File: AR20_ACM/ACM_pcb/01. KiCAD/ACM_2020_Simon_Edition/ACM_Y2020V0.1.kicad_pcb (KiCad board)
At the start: 2 copper layers, 18 x 22.5 mm, 32 parts, among them J1 TC2030-MCP-NL, P1 Conn_02x15_Odd_Even, Q1 Q_PMOS_DGS, U1 ATmega328P-AU, U2 MCP25625-x-SS, U3 NCV890430MW50TXG, Y1 16.0Mhz

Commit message: AtmegaFix
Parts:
- removed LED1: SMLP36RGB2W3R, SMLP36RGB2W3R:SMLP36RGB2W3R
- removed U1: ATmega328P-AU, Package_QFP:TQFP-32_7x7mm_P0.8mm
- added D3: ASMB-MTB0-0A3A2, LED_SMD:LED_Avago_PLCC4_3.2x2.8mm_CW, F.Cu at (118.9, 82.3)
- R3: value 200 Ohm -> 290 ohm
- R4: value 290 Ohm -> 200ohm
- moved R3 11.7 mm to (123.4, 81.1), turned to 0 degrees
- moved R4 10.8 mm to (123.4, 83.1), turned to 0 degrees
- moved R5 9.97 mm to (123.4, 85.1), turned to 0 degrees
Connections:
- net Net-(P1-Pad26) renamed /U-Pin26
- net Net-(P1-Pad28) renamed /U-Pin28
- C2 pad 1: +5V -> Net-(C2-Pad1)
- R3 pad 2: /GREEN_LED -> /RED_LED
- R4 pad 2: /RED_LED -> /GREEN_LED

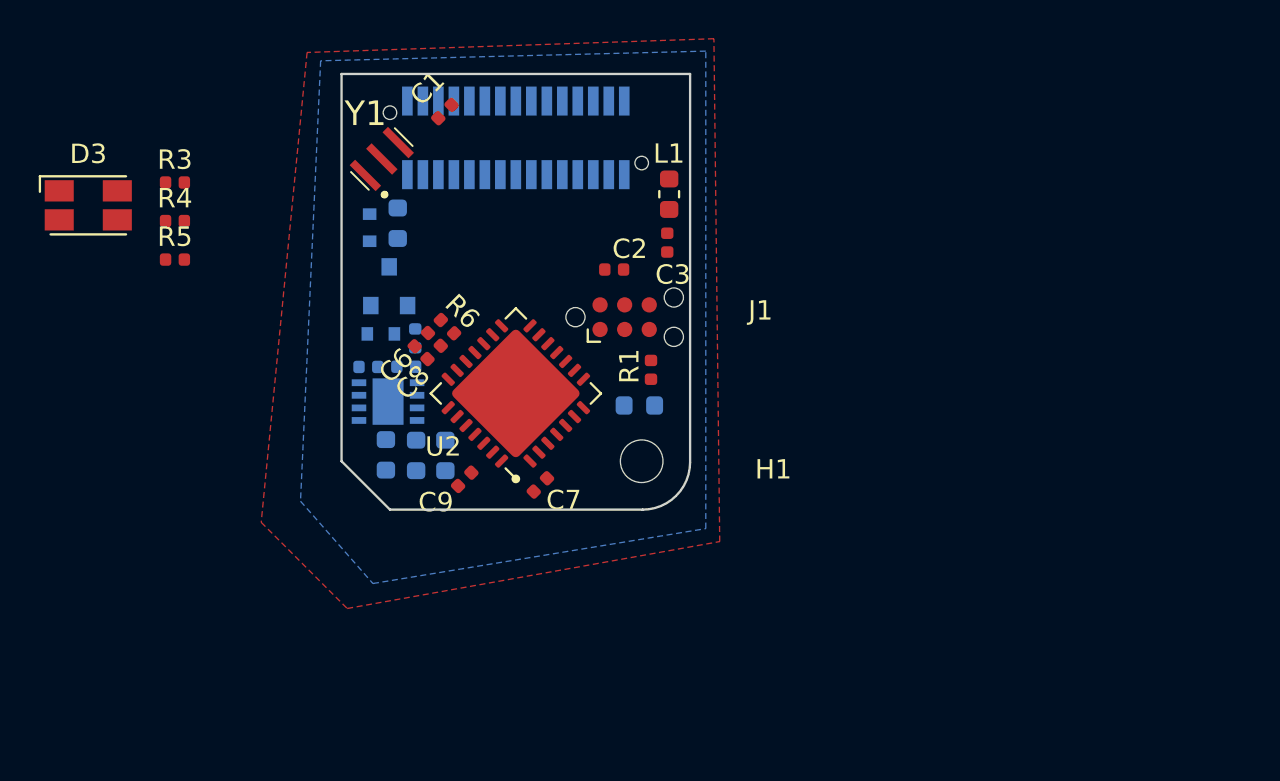
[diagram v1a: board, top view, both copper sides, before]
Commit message: Exploded and connected MCP25625 RX and TX
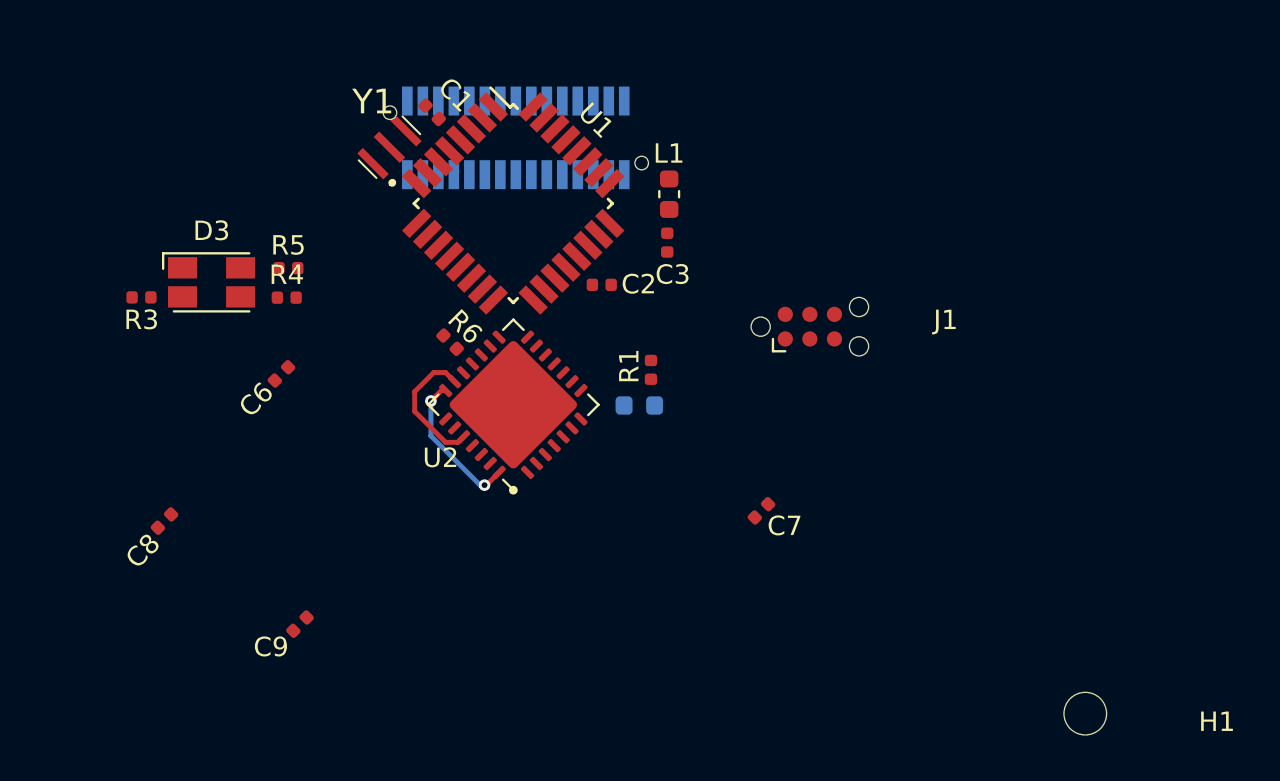
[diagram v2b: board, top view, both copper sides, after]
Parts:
- removed C10, C11: 10uF, Capacitor_SMD:C_0603_1608Metric
- removed C4, C5: 0.1uF, Capacitor_SMD:C_0402_1005Metric
- removed D1: 15V, Diode_SMD:D_SOD-523
- removed D2: 2.4V, Diode_SMD:D_SOD-523
- removed F1: 250mA, Fuse:Fuse_0603_1608Metric
- removed L2: 2.2 µH, Inductor_SMD:L_0603_1608Metric
- removed Q1: Q_PMOS_DGS, Package_TO_SOT_SMD:SOT-23
- removed R2: 100K Ohm, Resistor_SMD:R_0402_1005Metric
- removed U3: NCV890430MW50TXG, NCV890430MW50TXG:SON65P300X300X100-9N
- added U1: ATmega328P-AU, Package_QFP:TQFP-32_7x7mm_P0.8mm, F.Cu at (140.9, 82.2)
- moved H1 26.4 mm to (170.4, 108.5)
- moved C8 16.4 mm to (122.9, 98.6)
- moved C7 11.5 mm to (153.7, 98.1)
- moved C9 11.3 mm to (129.9, 103.9)
- moved J1 9.58 mm to (156.2, 88.6)
- moved D3 7.51 mm to (125.3, 86.3)
- moved C6 7.44 mm to (128.9, 91.0)
- moved R4 7.00 mm to (129.2, 87.1)
- moved R3 6.18 mm to (121.7, 87.0), turned to 180 degrees
- moved R5 5.87 mm to (129.3, 85.5)
- moved C2 1.02 mm to (145.4, 86.4)
- moved R6 0.81 mm to (137.6, 89.4)
- moved Y1 0.73 mm to (134.8, 79.6)
- moved C1 0.66 mm to (136.7, 77.5), turned to 135 degrees
- moved U2 0.60 mm to (140.9, 92.6)
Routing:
- net Net-(U2-Pad21): track 0.00 -> 7.64 mm, vias 0 -> 2
- net Net-(U2-Pad20): track 0.00 -> 6.99 mm
- removed copper zone on B.Cu, net +5V
- removed copper zone on F.Cu, net GND
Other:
- board outline removed
- board text removed: "[Optional]"
